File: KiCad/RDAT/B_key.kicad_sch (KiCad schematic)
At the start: 29 parts, among them J4 Bus_M.2_Socket_B, J7 SF72S006VBDR2500

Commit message: End Of day commit
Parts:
- J7: footprint Connector_JAE:JAE_SIM_Card_SF72S006 -> SF72S006VBDR2500_JAE
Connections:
- net GND: now also J4.P1 (GND), J4.P2 (GND)
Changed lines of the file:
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@@
 	)
 	(junction
-		(at 26.67 220.98)
+		(at 60.96 105.41)
 		(diameter 0)
 		(color 0 0 0 0)
 	)
 	(junction
-		(at 60.96 105.41)
+		(at 50.8 146.05)
 		(diameter 0)
 		(color 0 0 0 0)
 	)
 	(junction
-		(at 50.8 146.05)
+		(at 26.67 205.74)
 		(diameter 0)
 		(color 0 0 0 0)
 	)
 	(junction
-		(at 26.67 205.74)
+		(at 26.67 220.98)
 		(diameter 0)
 		(color 0 0 0 0)
@@
 	(wire
 		(pts
-			(xy 26.67 220.98) (xy 31.75 220.98)
-		)
-		(stroke
-			(width 0)
-			(type default)
-		)
-	)
-	(wire
-		(pts
 			(xy 107.95 54.61) (xy 107.95 64.77)
 		)
@@
 	(wire
 		(pts
-			(xy 26.67 223.52) (xy 26.67 224.79)
-		)
-		(stroke
-			(width 0)
-			(type default)
-		)
-	)
-	(wire
-		(pts
 			(xy 107.95 49.53) (xy 107.95 54.61)
 		)
@@
 	(wire
 		(pts
+			(xy 26.67 223.52) (xy 26.67 224.79)
+		)
+		(stroke
+			(width 0)
+			(type default)
+		)
+	)
+	(wire
+		(pts
 			(xy 54.61 92.71) (xy 60.96 92.71)
 		)
@@
 	(wire
 		(pts
-			(xy 31.75 223.52) (xy 26.67 223.52)
-		)
-		(stroke
-			(width 0)
-			(type default)
-		)
-	)
-	(wire
-		(pts
 			(xy 87.63 198.12) (xy 87.63 201.93)
 		)
@@
 	(wire
 		(pts
+			(xy 26.67 223.52) (xy 31.75 223.52)
+		)
+		(stroke
+			(width 0)
+			(type default)
+		)
+	)
+	(wire
+		(pts
 			(xy 17.78 114.3) (xy 29.21 114.3)
 		)
@@
 	(wire
 		(pts
+			(xy 26.67 220.98) (xy 26.67 223.52)
+		)
+		(stroke
+			(width 0)
+			(type default)
+		)
+	)
+	(wire
+		(pts
 			(xy 82.55 127) (xy 82.55 125.73)
 		)
@@
 	(wire
 		(pts
-			(xy 26.67 218.44) (xy 26.67 220.98)
+			(xy 58.42 140.97) (xy 58.42 146.05)
 		)
 		(stroke
@@
 	(wire
 		(pts
-			(xy 58.42 140.97) (xy 58.42 146.05)
+			(xy 26.67 218.44) (xy 26.67 220.98)
 		)
 		(stroke
@@
 	(wire
 		(pts
-			(xy 26.67 220.98) (xy 26.67 223.52)
+			(xy 46.99 146.05) (xy 50.8 146.05)
 		)
 		(stroke
@@
 	(wire
 		(pts
-			(xy 46.99 146.05) (xy 50.8 146.05)
+			(xy 138.43 140.97) (xy 133.35 140.97)
 		)
 		(stroke
@@
 	(wire
 		(pts
-			(xy 138.43 140.97) (xy 133.35 140.97)
+			(xy 26.67 220.98) (xy 31.75 220.98)
 		)
 		(stroke
@@
 		(pin "62"
 		)
+		(pin "P2"
+		)
+		(pin "P1"
+		)
 		(instances
 			(project "RDAT"
@@
 			)
 		)
-		(property "Footprint" "Connector_JAE:JAE_SIM_Card_SF72S006"
+		(property "Footprint" "SF72S006VBDR2500_JAE"
 			(at 31.75 187.96 0)
 			(effects
@@
 		(pin "C5"
 		)
-		(pin "GND9"
-		)
 		(pin "GND10"
 		)
-		(pin "GND8"
-		)
 		(pin "C2"
 		)
@@
 		(pin "GND7"
 		)
+		(pin "GND9"
+		)
+		(pin "GND8"
+		)
 		(instances

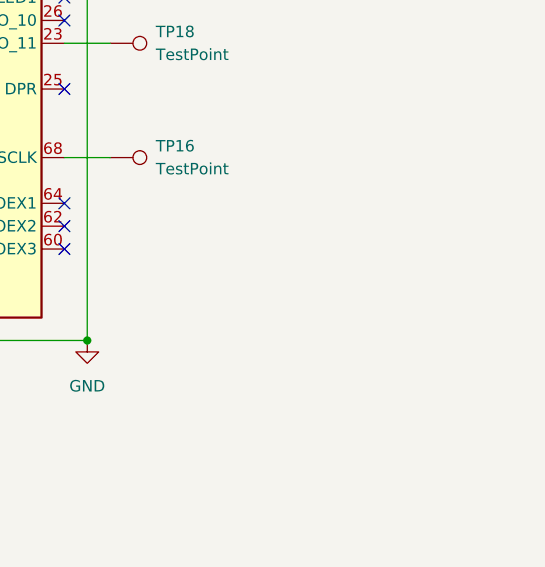
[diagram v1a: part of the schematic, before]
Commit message: Wrong footprint for keyswitches, creating save point
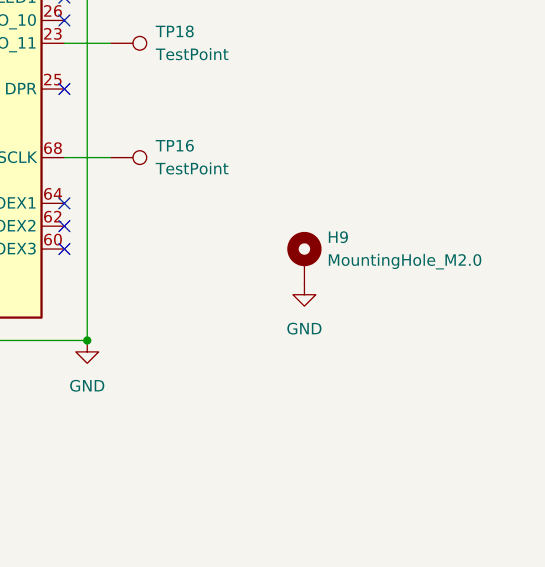
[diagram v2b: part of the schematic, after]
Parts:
- added H9: MountingHole_M2.0, MountingHole:MountingHole_2.2mm_M2_Pad_TopBottom, symbol Mechanical:MountingHole_Pad
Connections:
- net GND: now also H9.1
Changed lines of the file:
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@@
+	)
+	(symbol
+		(lib_id "power:GND")
+		(at 160.02 154.94 0)
+		(unit 1)
+		(exclude_from_sim no)
+		(in_bom yes)
+		(on_board yes)
+		(dnp no)
+		(fields_autoplaced yes)
+		(property "Reference" "#PWR084"
+			(at 160.02 161.29 0)
+			(effects
+				(font
+					(size 1.27 1.27)
+				)
+				(hide yes)
+			)
+		)
+		(property "Value" "GND"
+			(at 160.02 160.02 0)
+			(effects
+				(font
+					(size 1.27 1.27)
+				)
+			)
+		)
+		(property "Footprint" ""
+			(at 160.02 154.94 0)
+			(effects
+				(font
+					(size 1.27 1.27)
+				)
+				(hide yes)
+			)
+		)
+		(property "Datasheet" ""
+			(at 160.02 154.94 0)
+			(effects
+				(font
+					(size 1.27 1.27)
+				)
+				(hide yes)
+			)
+		)
+		(property "Description" ""
+			(at 160.02 154.94 0)
+			(effects
+				(font
+					(size 1.27 1.27)
+				)
+				(hide yes)
+			)
+		)
+		(pin "1"
+		)
+		(instances
+			(project "RDAT"
+				(path "/0db9370a-8a21-4fd2-83a9-f207c3725dc9/55ec8a2f-3960-4a3a-93a6-0eefb6fdb74b"
+					(reference "#PWR084")
+					(unit 1)
+				)
+			)
+		)
 	)
 	(symbol
@@
 					(unit 1)
 				)
+			)
+		)
+	)
+	(symbol
+		(lib_id "Mechanical:MountingHole_Pad")
+		(at 160.02 152.4 0)
+		(unit 1)
+		(exclude_from_sim no)
+		(in_bom yes)
+		(on_board yes)
+		(dnp no)
+		(fields_autoplaced yes)
+		(property "Reference" "H9"
+			(at 162.56 149.86 0)
+			(effects
+				(font
+					(size 1.27 1.27)
+				)
+				(justify left)
+			)
+		)
+		(property "Value" "MountingHole_M2.0"
+			(at 162.56 152.4 0)
+			(effects
+				(font
+					(size 1.27 1.27)
+				)
+				(justify left)
+			)
+		)
+		(property "Footprint" "MountingHole:MountingHole_2.2mm_M2_Pad_TopBottom"
+			(at 160.02 152.4 0)
+			(effects
+				(font
+					(size 1.27 1.27)
+				)
+				(hide yes)
+			)
+		)
+		(property "Datasheet" "~"
+			(at 160.02 152.4 0)
+			(effects
+				(font
+					(size 1.27 1.27)
+				)
+				(hide yes)
+			)
+		)
+		(property "Description" ""
+			(at 160.02 152.4 0)
+			(effects
+				(font
+					(size 1.27 1.27)
+				)
+				(hide yes)
+			)
+		)
+		(property "Sim.Device" ""
+			(at 160.02 152.4 0)
+			(effects
+				(font
+					(size 1.27 1.27)
+				)
+				(hide yes)
+			)
+		)
+		(property "Sim.Pins" ""
+			(at 160.02 152.4 0)
+			(effects
+				(font
+					(size 1.27 1.27)
+				)
+				(hide yes)
+			)
+		)
+		(property "Sim.Type" ""
+			(at 160.02 152.4 0)
+			(effects
+				(font
+					(size 1.27 1.27)
+				)
+				(hide yes)
+			)
+		)
+		(property "JLCPCB_LINK" ""
+			(at 160.02 152.4 0)
+			(effects
+				(font
+					(size 1.27 1.27)
+				)
+			)
+		)
+		(pin "1"
+		)
+		(instances
+			(project "RDAT"
+				(path "/0db9370a-8a21-4fd2-83a9-f207c3725dc9/55ec8a2f-3960-4a3a-93a6-0eefb6fdb74b"
+					(reference "H9")
+					(unit 1)
+				)

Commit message: 2x checing of bom on JLCPCB
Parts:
- C18: value 22uF/6.3V -> 22uF
- C19: value 10uF/6.3v -> 10uF
- C20, C21, C56: value 0.1uF/16v -> 0.1uF
- C57: value 1uF/6.3v -> 1uF
- C73: value 100fP/50v -> 100fP
- R78, R79, R83: JLCPCB_PART_NUMBER (none) -> C17168

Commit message: Generate Gerbers and Order PCB
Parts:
- C18: footprint Capacitor_SMD:C_0402_1005Metric -> Capacitor_SMD:C_0805_2012Metric; JLCPCB_LINK https://jlcpcb.com/partdetail/4414076-GRM158R61A226ME15D/C3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 -> https://jlcpcb.com/partdetail/46786-CL21A226MAQNNNE/C45783
- C19: JLCPCB_LINK https://jlcpcb.com/partdetail/16204-CL05A106MQ5NUNC/C15525 -> https://jlcpcb.com/partdetail/97651-CL10A106MA8NRNC/C96446
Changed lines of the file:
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@@
 			)
 		)
-		(property "Footprint" "Capacitor_SMD:C_0402_1005Metric"
+		(property "Footprint" "Capacitor_SMD:C_0805_2012Metric"
 			(at 115.57 57.15 0)
 			(effects
@@
 			)
 		)
-		(property "JLCPCB_LINK" "https://jlcpcb.com/partdetail/4414076-GRM158R61A226ME15D/C3845593"
+		(property "JLCPCB_LINK" "https://jlcpcb.com/partdetail/46786-CL21A226MAQNNNE/C45783"
 			(at 115.57 57.15 0)
 			(effects
@@
 			)
 		)
-		(property "JLCPCB_LINK" "https://jlcpcb.com/partdetail/16204-CL05A106MQ5NUNC/C15525"
+		(property "JLCPCB_LINK" "https://jlcpcb.com/partdetail/97651-CL10A106MA8NRNC/C96446"
 			(at 130.81 57.15 0)
 			(effects
